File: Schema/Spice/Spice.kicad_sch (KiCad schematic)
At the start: 5 parts, among them J1 Conn_02x03_Top_Bottom, U1 ATtiny85V-10P

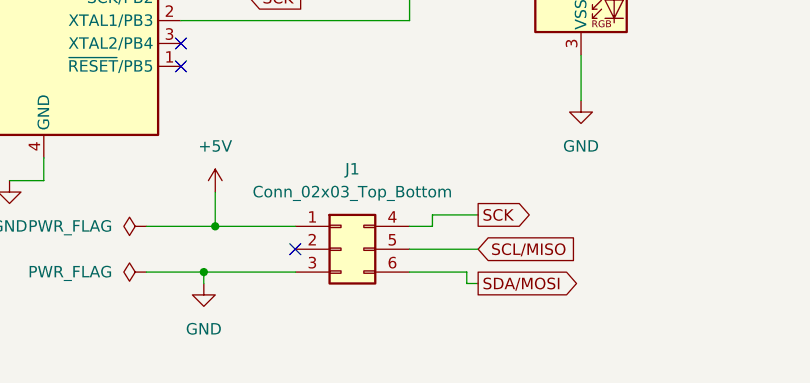
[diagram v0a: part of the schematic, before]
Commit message: Ändere Konnektor, korrigiere Pfadbreiten
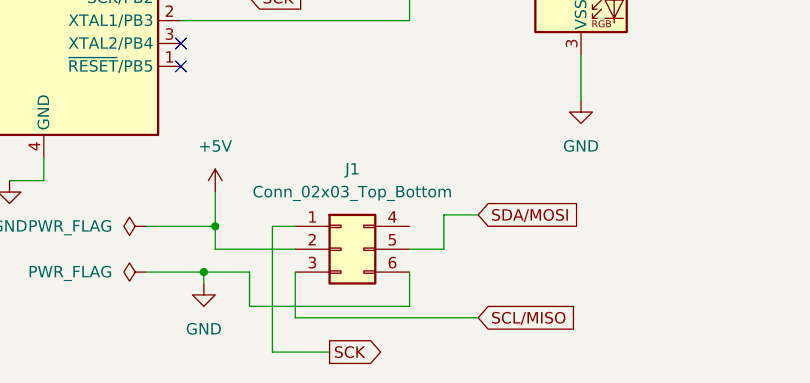
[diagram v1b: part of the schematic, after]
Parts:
- J1: footprint Connector_Molex:Molex_Mega-Fit_76829-0006_2x03_P5.70mm_Vertical -> Connector_IDC:IDC-Header_2x03_P2.54mm_Horizontal
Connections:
- net +5V: now also J1.2 (Pin_2); no longer J1.1 (Pin_1)
- net GND: now also J1.6 (Pin_6); no longer J1.3 (Pin_3)
- net SCK: now also J1.1 (Pin_1); no longer J1.4 (Pin_4)
- net SCL/MISO: now also J1.3 (Pin_3); no longer J1.5 (Pin_5)
- net SDA/MOSI: now also J1.5 (Pin_5); no longer J1.6 (Pin_6)
- no-connect marks 4 -> 3
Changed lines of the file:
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@@
-	)
-	(no_connect
-		(at 87.63 76.2)
 	)
 	(no_connect
@@
 	(wire
 		(pts
-			(xy 106.68 80.01) (xy 106.68 78.74)
-		)
-		(stroke
-			(width 0)
-			(type default)
-		)
-	)
-	(wire
-		(pts
-			(xy 100.33 76.2) (xy 107.95 76.2)
-		)
-		(stroke
-			(width 0)
-			(type default)
-		)
-	)
-	(wire
-		(pts
-			(xy 78.74 73.66) (xy 87.63 73.66)
+			(xy 87.63 83.82) (xy 87.63 78.74)
 		)
 		(stroke
@@
 	(wire
 		(pts
-			(xy 106.68 80.01) (xy 107.95 80.01)
+			(xy 87.63 83.82) (xy 107.95 83.82)
+		)
+		(stroke
+			(width 0)
+			(type default)
+		)
+	)
+	(wire
+		(pts
+			(xy 100.33 82.55) (xy 82.55 82.55)
 		)
 		(stroke
@@
 	(wire
 		(pts
+			(xy 82.55 78.74) (xy 77.47 78.74)
+		)
+		(stroke
+			(width 0)
+			(type default)
+		)
+	)
+	(wire
+		(pts
 			(xy 59.69 68.58) (xy 55.88 68.58)
 		)
@@
 	(wire
 		(pts
+			(xy 78.74 76.2) (xy 78.74 73.66)
+		)
+		(stroke
+			(width 0)
+			(type default)
+		)
+	)
+	(wire
+		(pts
+			(xy 85.09 87.63) (xy 91.44 87.63)
+		)
+		(stroke
+			(width 0)
+			(type default)
+		)
+	)
+	(wire
+		(pts
+			(xy 87.63 76.2) (xy 78.74 76.2)
+		)
+		(stroke
+			(width 0)
+			(type default)
+		)
+	)
+	(wire
+		(pts
 			(xy 199.39 31.75) (xy 199.39 39.37)
 		)
@@
 	(wire
 		(pts
+			(xy 100.33 78.74) (xy 100.33 82.55)
+		)
+		(stroke
+			(width 0)
+			(type default)
+		)
+	)
+	(wire
+		(pts
 			(xy 71.12 73.66) (xy 78.74 73.66)
 		)
@@
 	(wire
 		(pts
-			(xy 102.87 73.66) (xy 100.33 73.66)
-		)
-		(stroke
-			(width 0)
-			(type default)
-		)
-	)
-	(wire
-		(pts
-			(xy 102.87 72.39) (xy 102.87 73.66)
-		)
-		(stroke
-			(width 0)
-			(type default)
-		)
-	)
-	(wire
-		(pts
 			(xy 199.39 54.61) (xy 199.39 58.42)
 		)
@@
 	(wire
 		(pts
-			(xy 106.68 78.74) (xy 100.33 78.74)
-		)
-		(stroke
-			(width 0)
-			(type default)
-		)
-	)
-	(wire
-		(pts
 			(xy 119.38 31.75) (xy 119.38 39.37)
 		)
@@
 	(wire
 		(pts
-			(xy 107.95 72.39) (xy 102.87 72.39)
+			(xy 85.09 73.66) (xy 87.63 73.66)
 		)
 		(stroke
@@
 	(wire
 		(pts
-			(xy 77.47 78.74) (xy 87.63 78.74)
+			(xy 104.14 72.39) (xy 104.14 76.2)
+		)
+		(stroke
+			(width 0)
+			(type default)
+		)
+	)
+	(wire
+		(pts
+			(xy 85.09 87.63) (xy 85.09 73.66)
+		)
+		(stroke
+			(width 0)
+			(type default)
+		)
+	)
+	(wire
+		(pts
+			(xy 107.95 72.39) (xy 104.14 72.39)
 		)
 		(stroke
@@
 	(wire
 		(pts
+			(xy 104.14 76.2) (xy 100.33 76.2)
+		)
+		(stroke
+			(width 0)
+			(type default)
+		)
+	)
+	(wire
+		(pts
 			(xy 100.33 50.8) (xy 100.33 46.99)
 		)
@@
 		(pts
 			(xy 74.93 50.8) (xy 100.33 50.8)
+		)
+		(stroke
+			(width 0)
+			(type default)
+		)
+	)
+	(wire
+		(pts
+			(xy 82.55 82.55) (xy 82.55 78.74)
 		)
 		(stroke
@@
 	(global_label "SCL{slash}MISO"
 		(shape input)
-		(at 107.95 76.2 0)
+		(at 107.95 83.82 0)
 		(fields_autoplaced yes)
 		(effects
@@
 		)
 		(property "Intersheetrefs" "${INTERSHEET_REFS}"
-			(at 120.3695 76.2 0)
+			(at 120.3695 83.82 0)
 			(effects
 				(font
@@
 		)
 		(property "Netclass" "uC"
-			(at 107.95 78.3908 0)
+			(at 107.95 86.0108 0)
 			(effects
 				(font
@@
 	(global_label "SCK"
 		(shape output)
-		(at 107.95 72.39 0)
+		(at 91.44 87.63 0)
 		(fields_autoplaced yes)
 		(effects
@@
 		)
 		(property "Intersheetrefs" "${INTERSHEET_REFS}"
-			(at 114.6847 72.39 0)
+			(at 98.1747 87.63 0)
 			(effects
 				(font
@@
 		)
 		(property "Netclass" "uC"
-			(at 107.95 74.5808 0)
+			(at 91.44 89.8208 0)
 			(effects
 				(font
@@
 	)
 	(global_label "SDA{slash}MOSI"
-		(shape output)
-		(at 107.95 80.01 0)
+		(shape input)
+		(at 74.93 34.29 90)
 		(fields_autoplaced yes)
 		(effects
@@
 		)
 		(property "Intersheetrefs" "${INTERSHEET_REFS}"
-			(at 120.43 80.01 0)
-			(effects
-				(font
-					(size 1.27 1.27)
-				)
-				(justify left)
-				(hide yes)
-			)
-		)
-		(property "Netclass" "uC"
-			(at 107.95 82.2008 0)
+			(at 74.93 21.81 90)
 			(effects
 				(font
@@
 	(global_label "SDA{slash}MOSI"
 		(shape input)
-		(at 74.93 34.29 90)
+		(at 107.95 72.39 0)
 		(fields_autoplaced yes)
 		(effects
@@
 		)
 		(property "Intersheetrefs" "${INTERSHEET_REFS}"
-			(at 74.93 21.81 90)
+			(at 120.43 72.39 0)
 			(effects
 				(font
@@
 			)
 		)
-		(property "Footprint" "Connector_Molex:Molex_Mega-Fit_76829-0006_2x03_P5.70mm_Vertical"
+		(property "Footprint" "Connector_IDC:IDC-Header_2x03_P2.54mm_Horizontal"
 			(at 92.71 76.2 0)
 			(effects

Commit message: Räume Schema auf
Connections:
- no-connect marks 3 -> 4

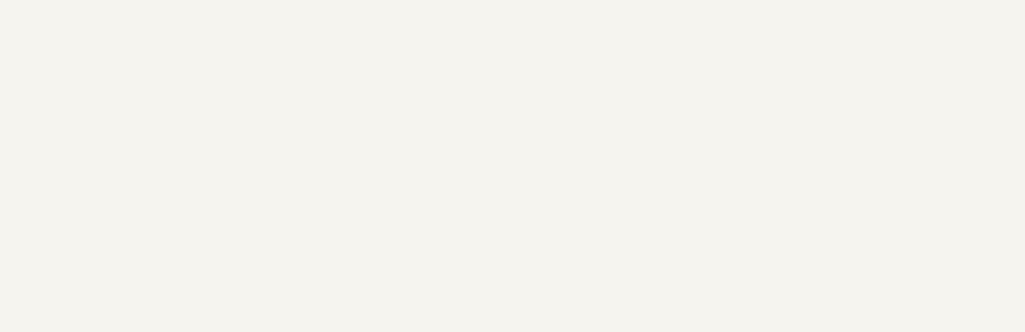
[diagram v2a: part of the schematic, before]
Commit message: Verkleinere die Fläche, füge Bohrungen ein
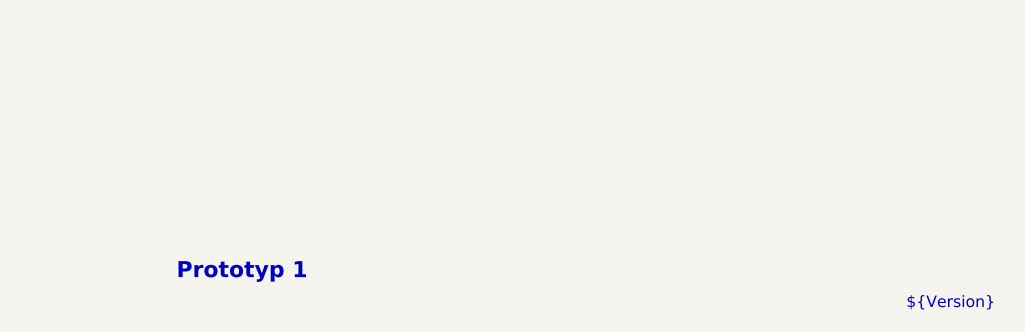
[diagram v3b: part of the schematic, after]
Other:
- note added: "${Version}"
- note added: "Prototyp 1"
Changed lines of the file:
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@@
 	(generator_version "9.0")
 	(paper "A4")
+	(text "Prototyp 1"
+		(exclude_from_sim no)
+		(at 194.564 189.738 0)
+		(effects
+			(font
+				(size 1.778 1.778)
+				(thickness 0.3556)
+				(bold yes)
+			)
+		)
+	)
+	(text "${Version}"
+		(exclude_from_sim no)
+		(at 273.304 193.294 0)
+		(effects
+			(font
+				(size 1.27 1.27)
+			)
+		)
+	)
 	(junction
 		(at 74.93 73.66)
